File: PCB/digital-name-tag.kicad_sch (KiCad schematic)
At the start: 39 parts, among them J1 USB_C_Receptacle_USB2.0_14P, J2 Conn_01x20, J3 Conn_01x20, J4 Conn_01x03, Q1 DMG1012T, SW1 SW_Push, U1 RP2040, U2 MCP1700x-120xxMB, U3 W25Q128JVS, Y1 12MHz

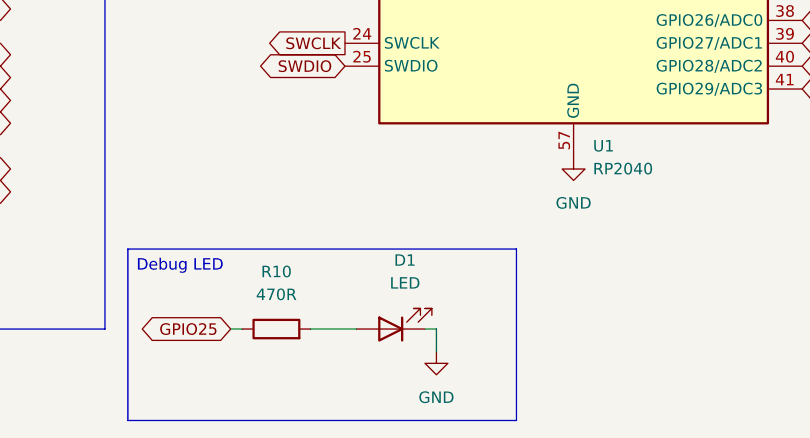
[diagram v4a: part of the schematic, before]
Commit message: fixed BOM and got the pcb added to cart I think i forgot to save the BOM last time but i ended up changing a good portion of it anyways to change from exstended pcba to basic.
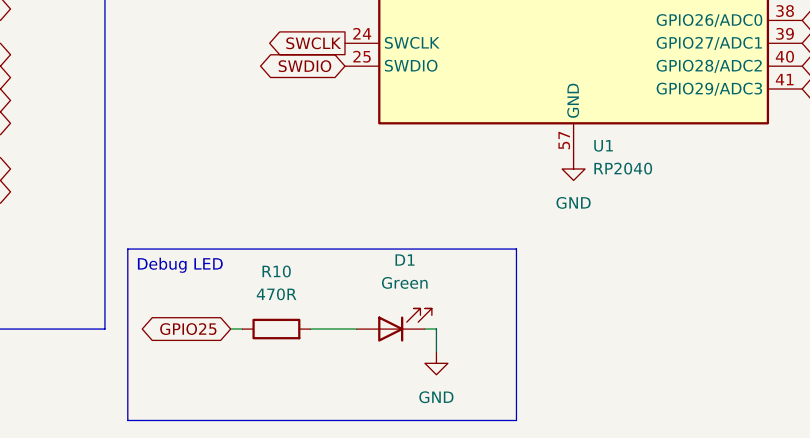
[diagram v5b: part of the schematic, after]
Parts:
- D1: value LED -> Green
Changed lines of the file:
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@@
 			)
 		)
-		(property "Value" "LED"
+		(property "Value" "Green"
 			(at 128.5875 175.26 0)
 			(effects

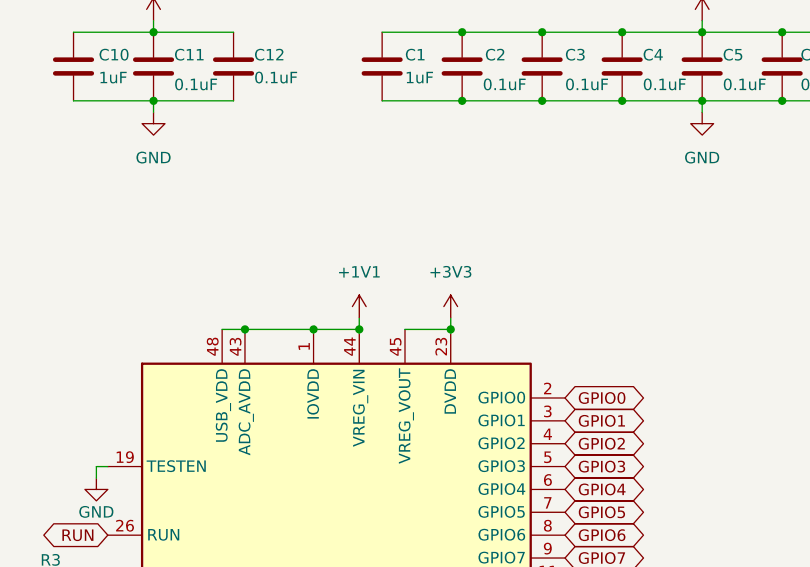
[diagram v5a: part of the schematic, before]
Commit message: updated the schematic and pcb to have the correct power rails.
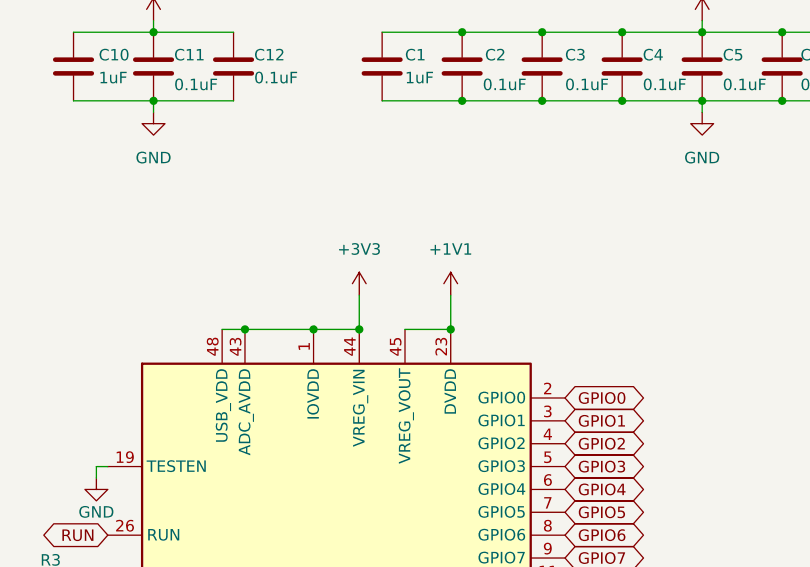
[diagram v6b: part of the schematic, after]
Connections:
- net +1V1: now also U1.23 (DVDD), U1.45 (VREG_VOUT), U1.50 (DVDD); no longer U1.1 (IOVDD), U1.10 (IOVDD), U1.22 (IOVDD), U1.33 (IOVDD), U1.42 (IOVDD), U1.43 (ADC_AVDD), U1.44 (VREG_VIN), U1.48 (USB_VDD), U1.49 (IOVDD)
- net +3V3: now also U1.1 (IOVDD), U1.10 (IOVDD), U1.22 (IOVDD), U1.33 (IOVDD), U1.42 (IOVDD), U1.43 (ADC_AVDD), U1.44 (VREG_VIN), U1.48 (USB_VDD), U1.49 (IOVDD); no longer U1.23 (DVDD), U1.45 (VREG_VOUT), U1.50 (DVDD)
